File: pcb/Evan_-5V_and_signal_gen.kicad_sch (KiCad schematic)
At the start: 35 parts, among them IC1 TL7660IDGKR, IC2 TL081IDT, IC4 UA78M33CDCYG3, U2 LTC4300A-1IMS8_PBF, U5 TPS2069CDBVR_MOSFET

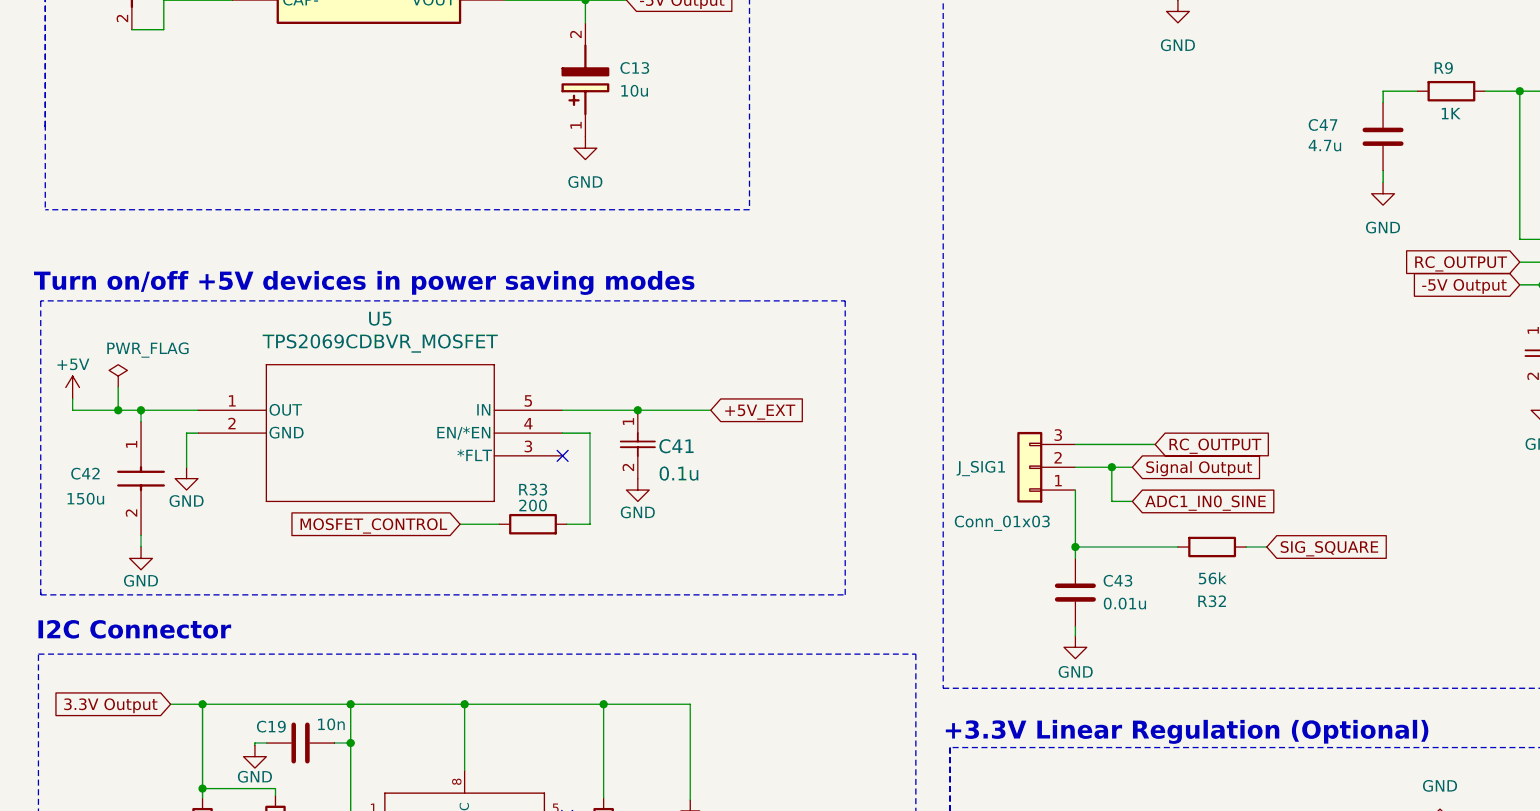
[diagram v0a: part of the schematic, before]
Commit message: Thermal Reliefs for Shields
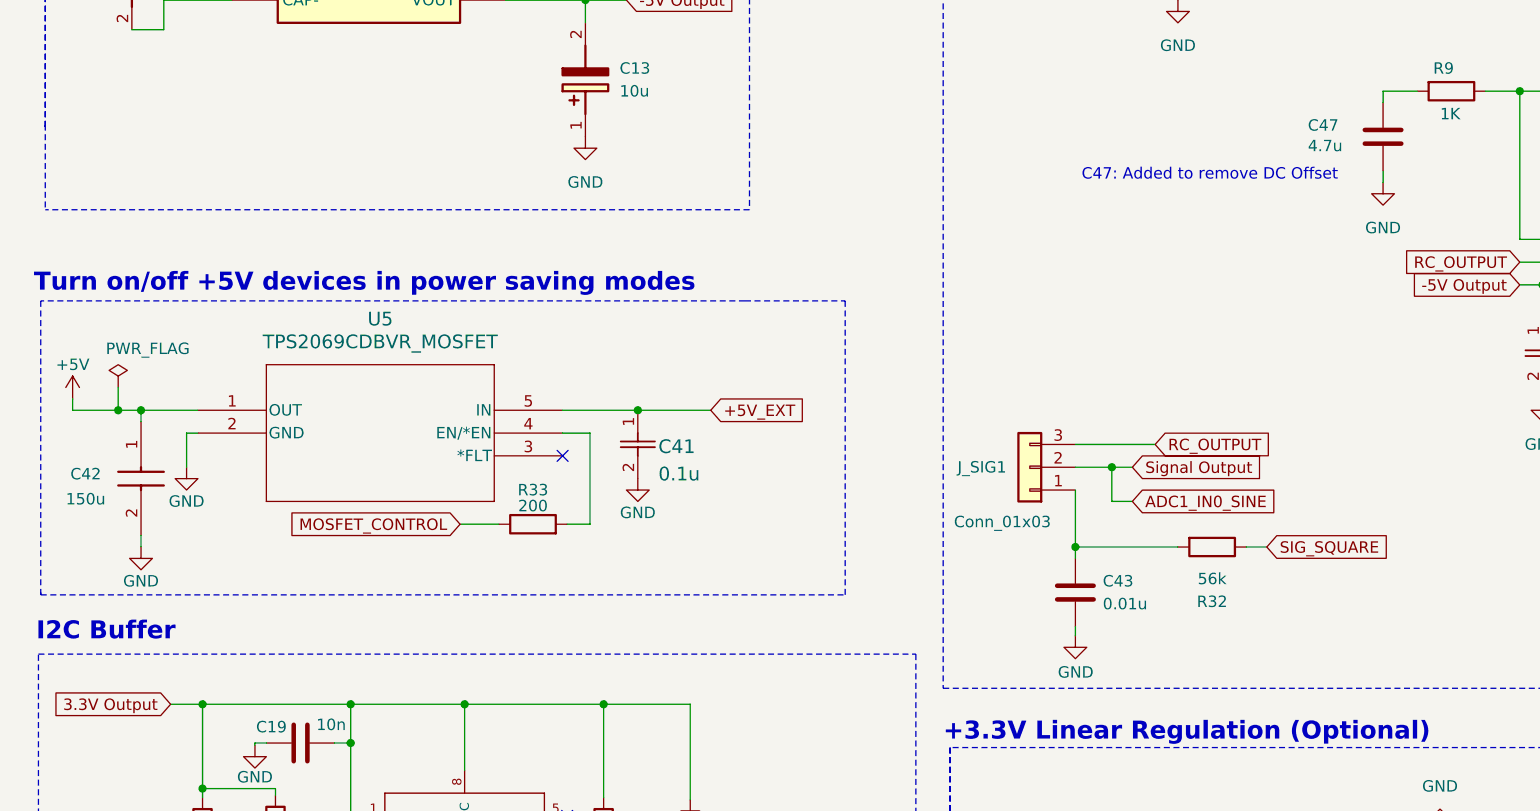
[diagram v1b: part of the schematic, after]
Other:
- note added: "C47: Added to remove DC Offset"
- note added: "I2C Buffer"
- note removed: "I2C Connector"
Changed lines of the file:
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@@
+		)
+	)
+	(text "C47: Added to remove DC Offset"
+		(exclude_from_sim no)
+		(at 147.066 58.928 0)
+		(effects
+			(font
+				(size 1.27 1.27)
+			)
 		)
 	)
@@
 		)
 	)
-	(text "I2C Connector"
+	(text "I2C Buffer"
 		(exclude_from_sim no)
 		(at 16.256 110.998 0)

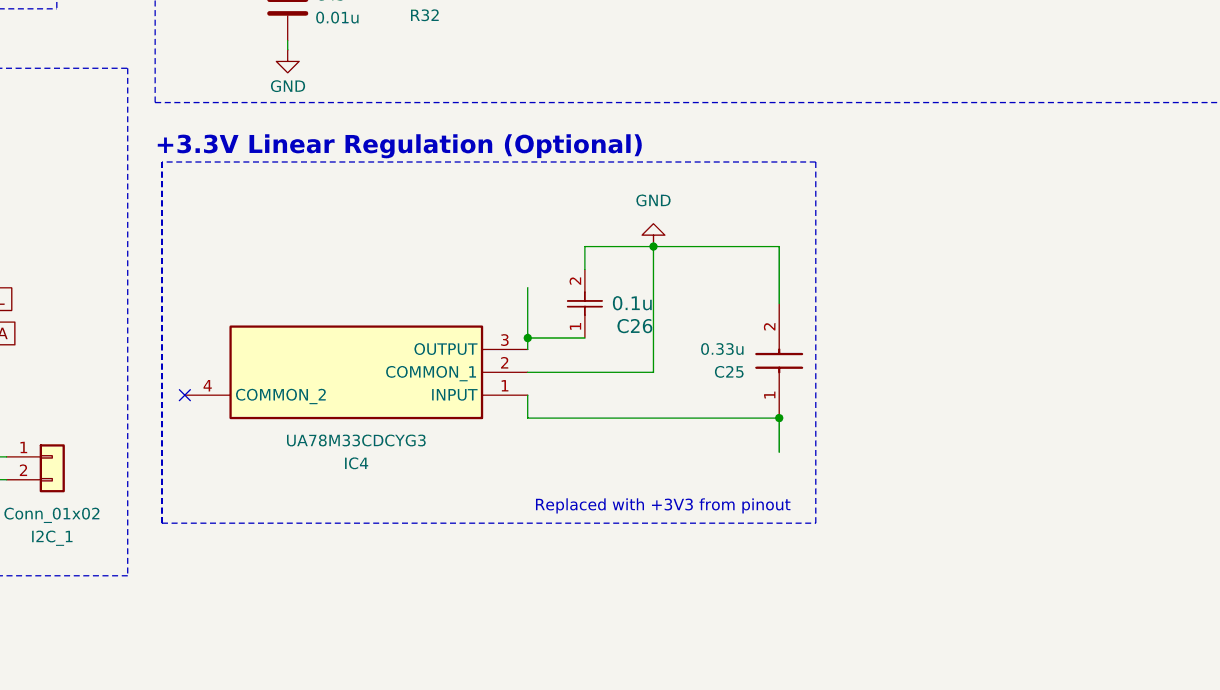
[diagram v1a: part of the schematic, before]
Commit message: Added 3V3 linear voltage regulator
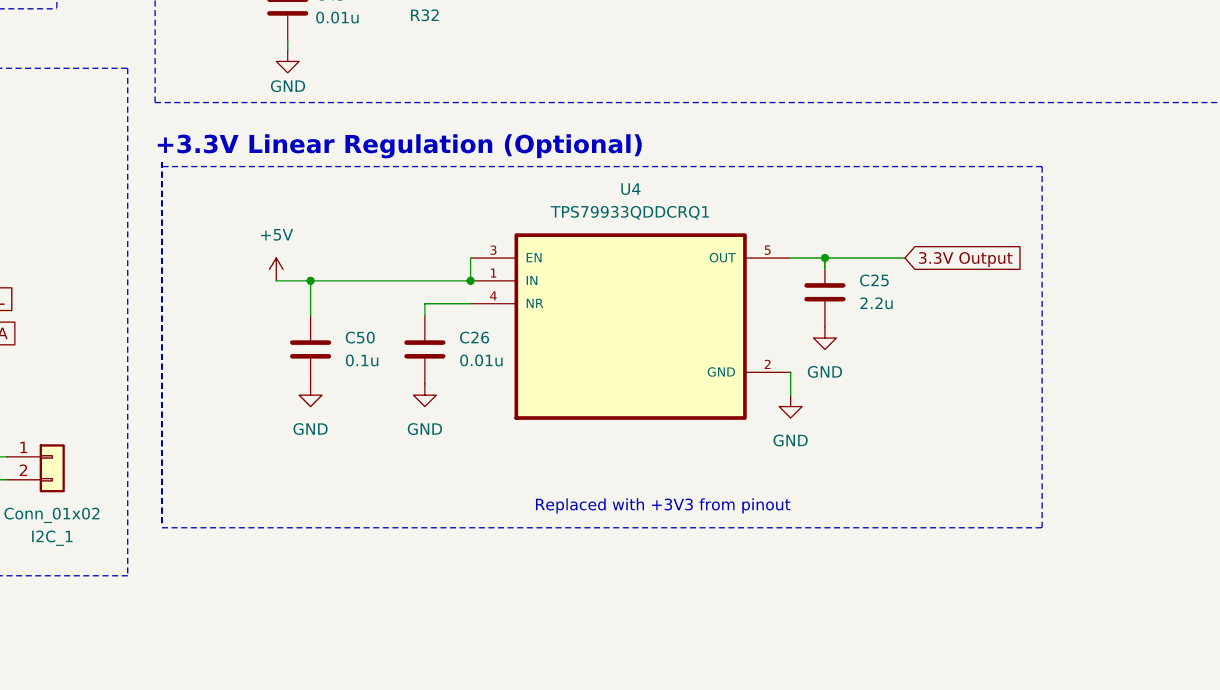
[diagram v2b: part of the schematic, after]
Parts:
- removed C25: 0.33u, capstone:C0805, symbol capstone:C0805C334K3RACAUTO7210
- removed C26: 0.1u, capstone:CAPC220145_88N_KEM-0.1u, symbol capstone:C0805C104K5RAC7210
- removed IC4: UA78M33CDCYG3, capstone:SOT230P700X180-4N, symbol capstone:UA78M33CDCYG3
- added C25: 2.2u, Capacitor_SMD:C_0402_1005Metric, symbol Device:C
- added C26: 0.01u, Capacitor_SMD:C_0402_1005Metric, symbol Device:C
- added C50: 0.1u, Capacitor_SMD:C_0402_1005Metric, symbol Device:C
- added U4: TPS79933QDDCRQ1, TPS79933QDDCRQ1 (1):SOT95P280X110-5N, symbol TPS79933QDDCRQ1:TPS79933QDDCRQ1
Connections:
- net +5V: now also C50.1, U4.1 (IN), U4.3 (EN)
- net 3.3V Output: now also C25.1, U4.5 (OUT)
- net GND: now also C25.2, C26.2, C50.2, U4.2 (GND)
- new net: C26.1, U4.4 (NR)
- no-connect marks 6 -> 5
